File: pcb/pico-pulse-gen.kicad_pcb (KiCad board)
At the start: 2 copper layers, 100 x 100 mm, 58 parts, among them J1 MOTM_PWR, J2 PWR_CON, J3 OUT_CON, J4 EXT_CLK, SW1 P1_BTN, SW10 P8_BTN, SW11 OUT1_BTN, SW12 OUT2_BTN, SW13 OUT3_BTN, SW2 P2_BTN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

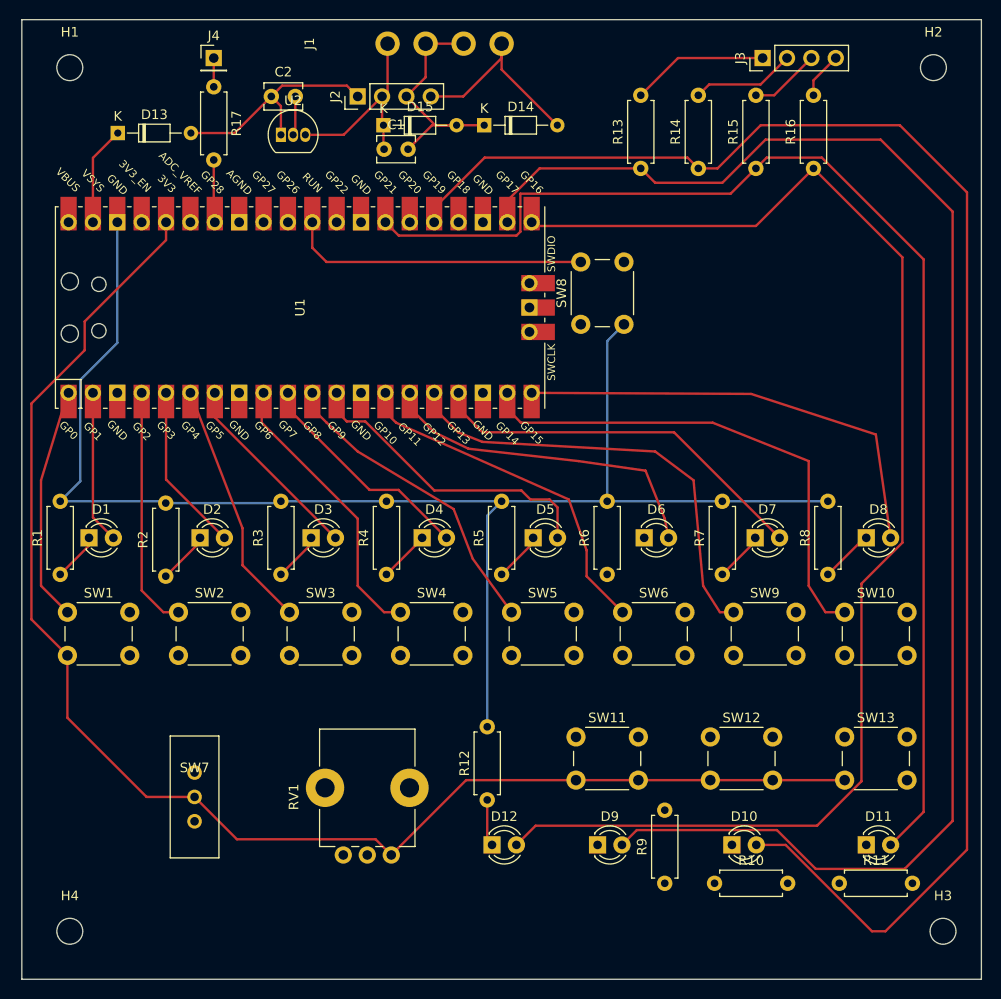
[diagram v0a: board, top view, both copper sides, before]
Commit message: feat: routed pcb
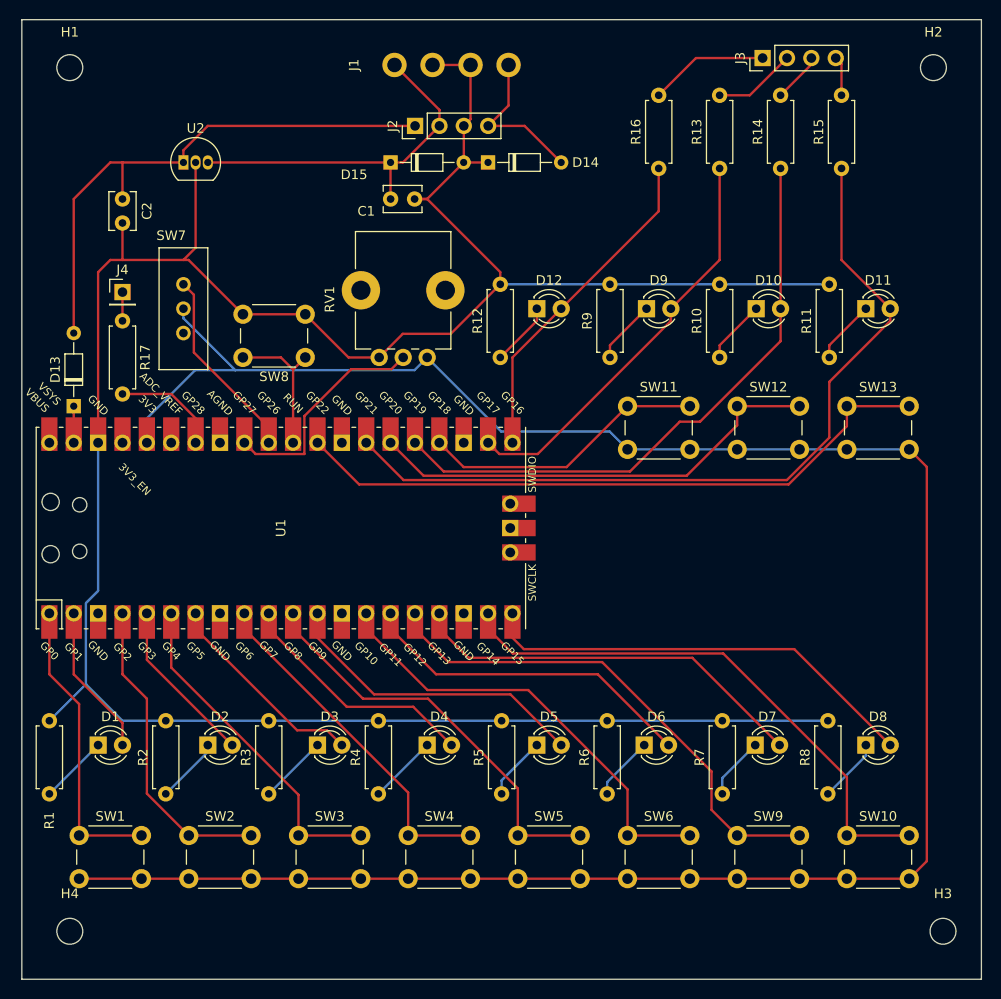
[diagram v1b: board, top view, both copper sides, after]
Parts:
- moved D9 56.1 mm to (165.1, 71.1)
- moved D12 56.1 mm to (153.7, 71.1)
- moved D10 55.9 mm to (176.5, 71.1)
- moved D11 55.9 mm to (188.0, 71.1)
- moved R9 55.1 mm to (161.3, 76.2)
- moved R11 54.8 mm to (184.2, 76.2), turned to 90 degrees
- moved R10 54.8 mm to (172.7, 76.2), turned to 90 degrees
- moved RV1 52.0 mm to (142.2, 76.2)
- moved SW7 50.9 mm to (116.8, 68.6)
- moved R12 46.1 mm to (149.9, 76.2)
- moved SW11 34.9 mm to (163.1, 81.3)
- moved SW12 34.6 mm to (174.6, 81.3)
- moved SW13 34.5 mm to (186.0, 81.3)
- moved SW8 28.9 mm to (129.5, 76.2), turned to 180 degrees
- moved D13 28.8 mm to (105.4, 81.3), turned to 90 degrees
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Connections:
- R13 pad 2: Net-(J3-Pad1) -> Net-(J3-Pad2)
- R14 pad 2: Net-(J3-Pad2) -> Net-(J3-Pad3)
- R15 pad 2: Net-(J3-Pad3) -> Net-(J3-Pad4)
- R16 pad 2: Net-(J3-Pad4) -> Net-(J3-Pad1)
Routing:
- net /GPIO17: track 158.0 -> 43.3 mm
- net /GPIO16: track 140.2 -> 34.9 mm
- net /GPIO19: track 162.1 -> 63.0 mm
- net +3V3: track 149.2 -> 230.0 mm
- net GND: track 184.8 -> 263.4 mm
- net /GPIO22: track 0.00 -> 68.1 mm
- net /GPIO20: track 0.00 -> 48.2 mm
- net /GPIO21: track 129.2 -> 84.5 mm
- net +5V: track 24.3 -> 57.3 mm
- net /GPIO18: track 0.00 -> 29.8 mm
- net Net-(RV1-Pad2): track 0.00 -> 23.5 mm
- net Net-(SW7-Pad1): track 0.00 -> 20.2 mm
- net +15V: track 21.0 -> 37.8 mm
- net Net-(SW8-Pad1): track 31.3 -> 15.2 mm
- net /GPIO8: track 32.2 -> 43.3 mm
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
